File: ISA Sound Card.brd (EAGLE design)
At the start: 175.9 x 108.6 mm, 60 parts, among them IC1 74LS07D, IC2 74AHC1G07DBV, U1 PCM1808, U10 SN74LVC16T245DGGR, U11 SN74LVC16T245DGGR, U12 SN74LVC16T245DGGR, U3 MIC5365-3.3YD5-TR, U4 PCM5102, U5 SN74LVC16T245DGGR, U7 MIC5365-3.3YD5-TR, U8 SN74LVC16T245DGGR, U9 SN74LVC16T245DGGR, X2 LINE_OUT, X3 LINE_IN

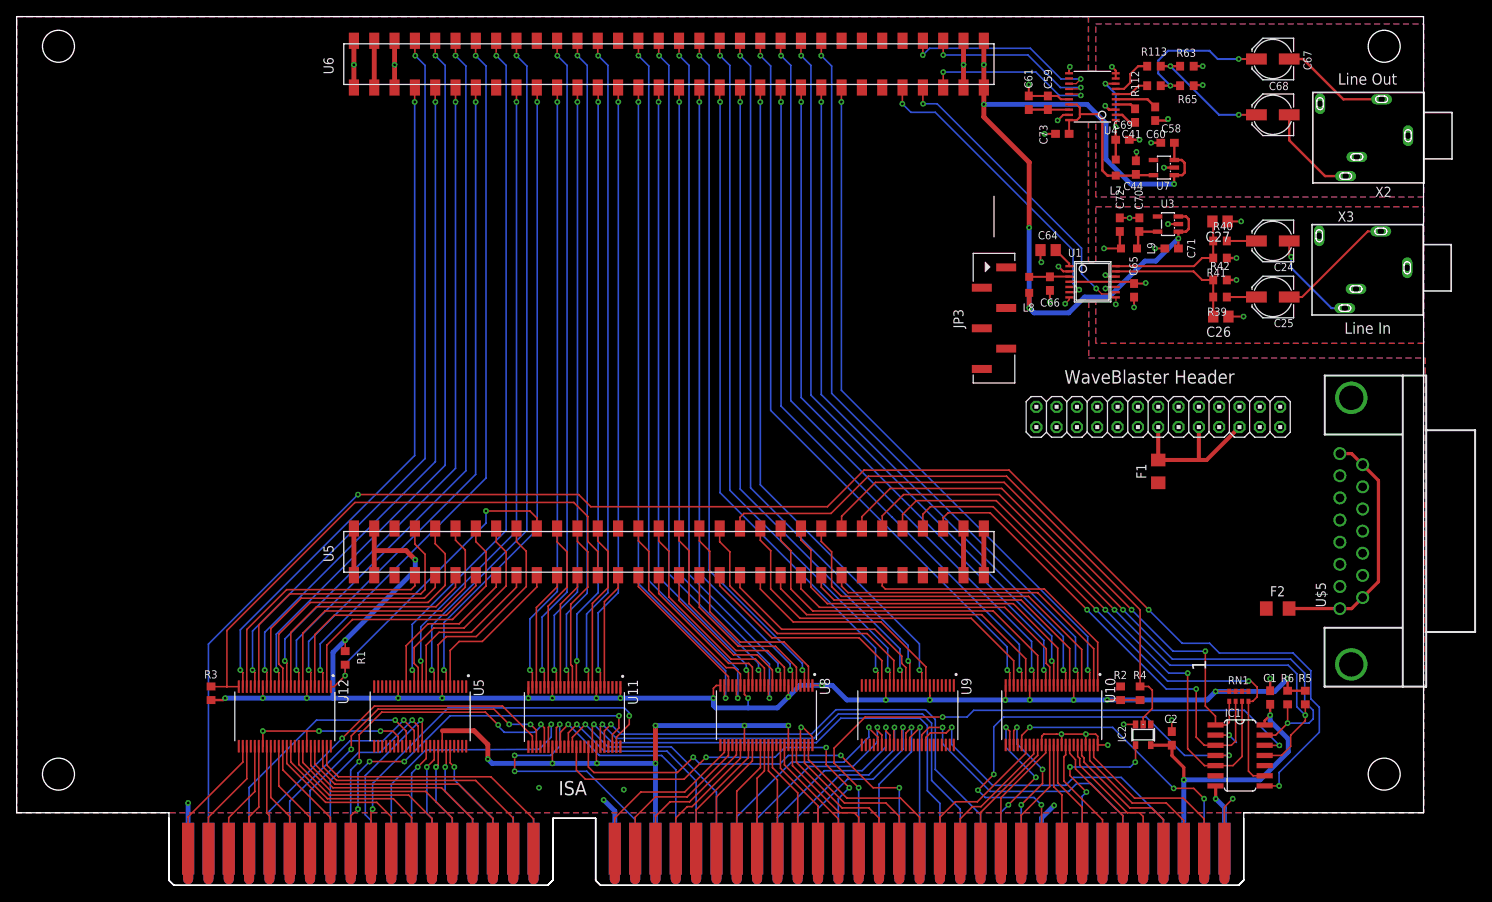
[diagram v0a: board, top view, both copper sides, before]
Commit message: First routing done, DRC passed. MIDI and Waveblaster are todo
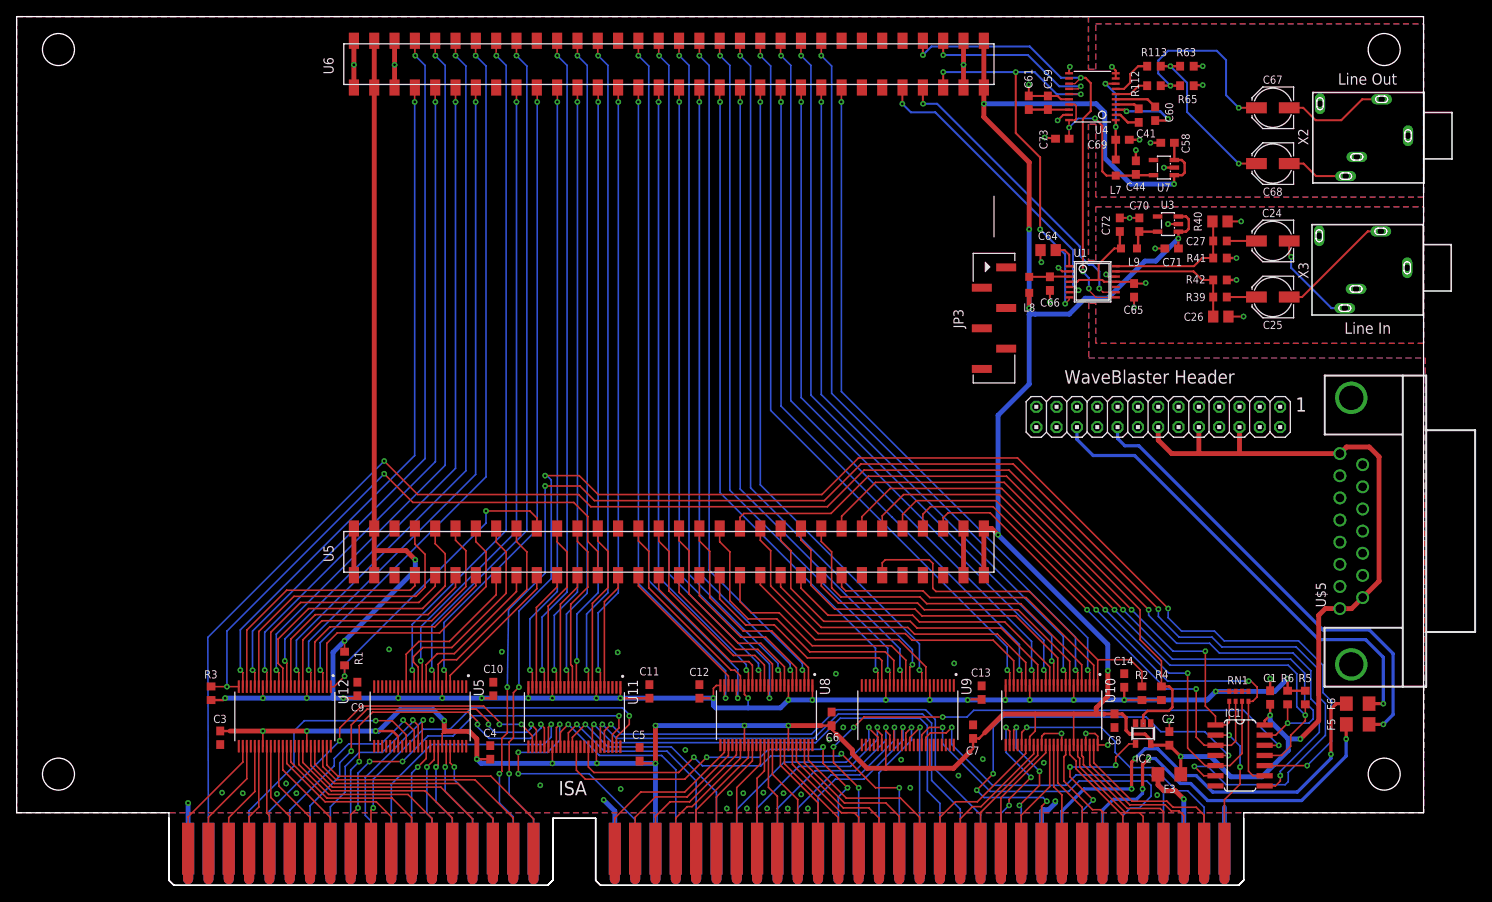
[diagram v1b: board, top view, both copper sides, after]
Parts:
- removed F1, F2: 500mA, adafruit:R1206
- added C10, C11, C12, C13, C14, C3, C4, C5, C6, C7, C8, C9: 100nF, rcl:C0603
- added F3, F5, F6: 500mA, adafruit:R1206
- moved C67 6.10 mm to (165.0, 105.5)
- moved C68 6.10 mm to (165.0, 98.5)
- moved R2 2.67 mm to (148.6, 32.3)
- moved R4 2.67 mm to (151.0, 32.3)
- moved C73 0.61 mm to (138.6, 101.6)
- moved C41 0.46 mm to (148.2, 104.5)
- moved C2 0.30 mm to (152.0, 26.7)
- moved IC2 0.15 mm to (148.7, 27.3)
- moved R1 0.11 mm to (48.9, 36.7)
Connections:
- net -5V renamed -5VDC
- new net MIDI_RXD: U$5.12
- new net MIDI_TXD: U$5.15
- new net N$13: F3.2, ISA.B3
- new net N$14: F5.2, ISA.B7
- new net N$27: F6.2, ISA.B9
- net +12V: now also F5.1; no longer ISA.B7
- net +3V3: now also C10.1, C11.1, C12.1, C13.1, C14.1, C9.1
- net +5V: now also C3.1, C4.1, C5.1, C6.1, C7.1, C8.1, F3.1, JP1.10, JP1.14, JP1.6, U$5.1, U$5.8, U$5.9; no longer F1.2, F2.2, ISA.B3
- net -12V: now also F6.1; no longer ISA.B9
- net GND: now also C10.2, C11.2, C12.2, C13.2, C14.2, C3.2, C4.2, C5.2, C6.2, C7.2, C8.2, C9.2; no longer U$5.12
- net N$5: now also U$1.1; no longer F1.1, JP1.10, JP1.14, JP1.6
- net N$6: now also U$1.5; no longer F2.1, U$5.1, U$5.15, U$5.8, U$5.9
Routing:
- net +5V: track 244.5 -> 467.2 mm, vias 18 -> 21
- net I/!OCS16: track 3.99 -> 191.1 mm, vias 0 -> 5
- net !MEMCS16: track 3.73 -> 181.6 mm, vias 0 -> 5
- net +3V3: track 219.3 -> 286.7 mm, vias 23 -> 26
- net -12V: track 0.00 -> 58.7 mm, vias 0 -> 1
- net +12V: track 0.00 -> 58.1 mm, vias 0 -> 1
- net N$27: track 0.00 -> 55.9 mm, vias 0 -> 3
- net N$14: track 0.00 -> 48.5 mm, vias 0 -> 3
- net N$6: track 31.4 -> 0.00 mm
- net I2S_LRCK: track 22.9 -> 54.3 mm, vias 3 -> 5
- net I2S_BCK: track 26.0 -> 57.2 mm, vias 3 -> 4
- net N$5: track 20.1 -> 0.00 mm
- net GND: track 118.6 -> 105.6 mm, vias 40 -> 66
- net N$13: track 0.00 -> 11.5 mm, vias 0 -> 1
- net FPGA_SD70_DIR: track 36.6 -> 46.9 mm
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
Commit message: Had to change IRQ/DRQ buffers for muxes. Not routed yet
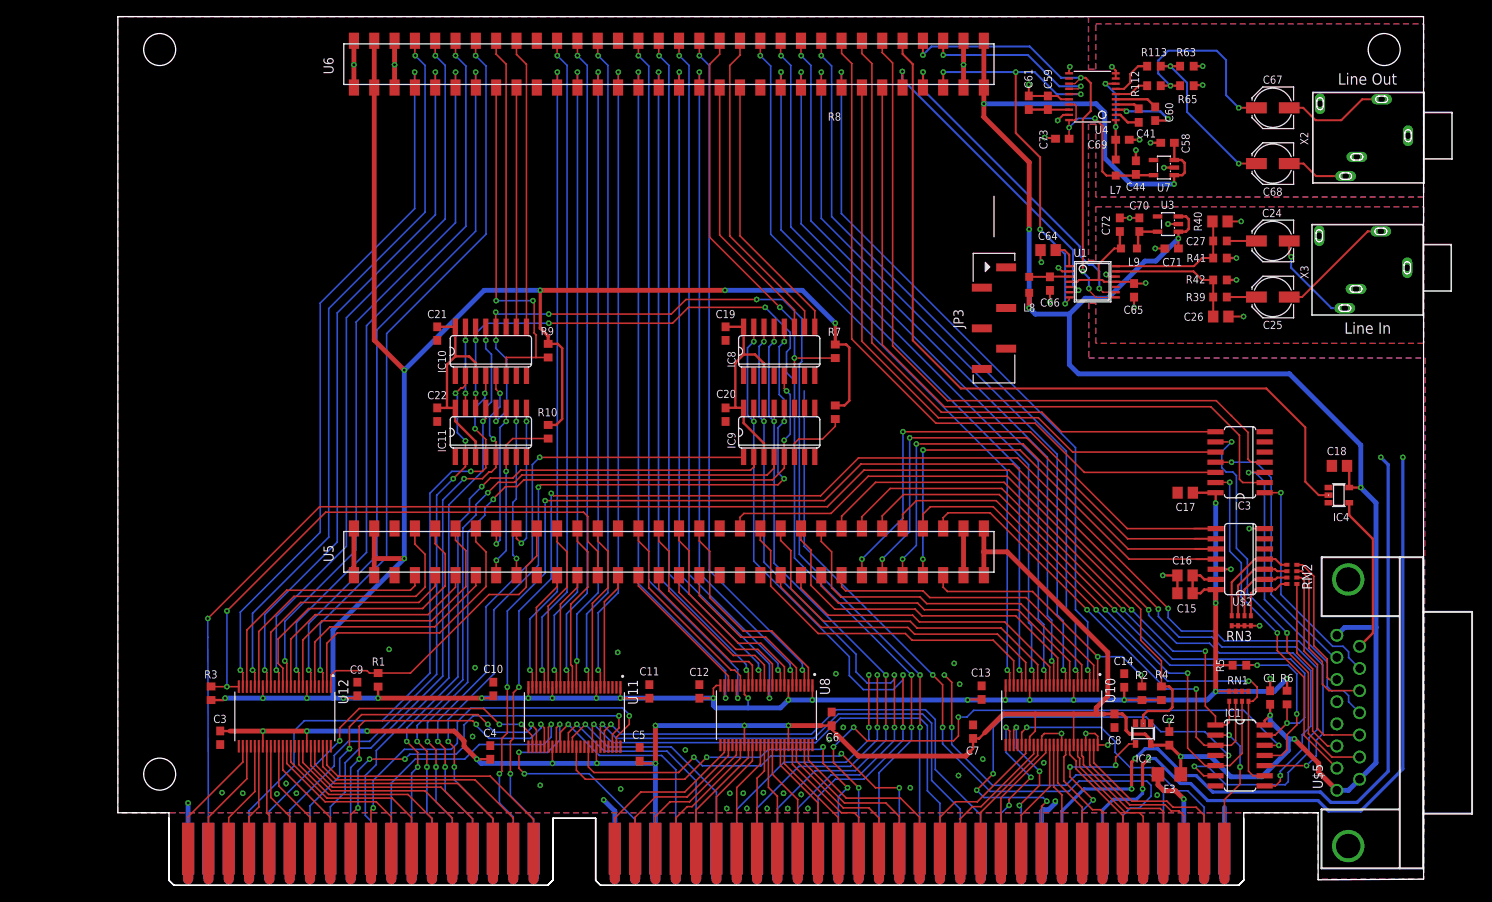
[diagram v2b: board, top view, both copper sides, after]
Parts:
- removed F5, F6: 500mA, adafruit:R1206
- removed JP1: (no value), pinhead:2X13
- removed U5, U9: SN74LVC16T245DGGR, SN74LVC16T245DGGR:SOP50P810X120-48N
- added C15, C16, C17, C18: 100nF, rcl:C0805
- added C19, C20, C21, C22: 100nF, rcl:C0603
- added IC10, IC11, IC8, IC9: 4051D, 40xx:SO16
- added IC3: 74AC14D, 74xx-eu:SO14
- added IC4: 74LVC1G125DBV, 74xx-little-de:SOT23-5
- added R10, R7, R8, R9: 4K7, rcl:R0603
- added RN2: 10K, resistor-dil:0603-ARC
- added RN3: 2K2, resistor-dil:0603-ARC
- added U$2: MCP3004, adafruit:SO14
- RN1: value (none) -> 2K2
- moved U$5 22.7 mm to (174.4, 29.9)
- moved R5 9.17 mm to (160.8, 35.8), turned to 0 degrees
- moved R1 4.97 mm to (53.1, 34.0), turned to 90 degrees
- moved R6 0.08 mm to (166.7, 31.8)
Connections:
- net N$5 renamed FPGA_DCLK
- net N$6 renamed FPGA_ADS0
- removed net +12V: F5.1, JP1.18
- removed net -12V: F6.1, JP1.22
- removed net FPGA_DRQ0: U$1.U6_17, U5.12
- removed net FPGA_DRQ1: U$1.U5_39, U9.13
- removed net FPGA_DRQ2: U$1.U6_41, U9.9
- removed net FPGA_DRQ3: U$1.U6_40, U9.12
- removed net FPGA_DRQ5: U$1.U5_16, U5.13
- removed net FPGA_DRQ6: U$1.U6_16, U5.14
- removed net FPGA_DRQ7: U$1.U5_15, U5.16
- removed net FPGA_IRQ10: U$1.U5_19, U5.5
- removed net FPGA_IRQ11: U$1.U6_19, U5.6
- removed net FPGA_IRQ12: U$1.U5_18, U5.8
- removed net FPGA_IRQ14: U$1.U5_17, U5.11
- removed net FPGA_IRQ15: U$1.U6_18, U5.9
- removed net FPGA_IRQ3: U$1.U6_37, U9.20
- removed net FPGA_IRQ4: U$1.U5_37, U9.19
- removed net FPGA_IRQ5: U$1.U6_38, U9.17
- removed net FPGA_IRQ6: U$1.U5_38, U9.16
- removed net FPGA_IRQ7: U$1.U6_39, U9.14
- removed net FPGA_IRQ9: U$1.U5_41, U9.8
- removed net GAME_B1_N: U$5.2
- removed net GAME_B2_N: U$5.7
- removed net GAME_B3_N: U$5.10
- removed net GAME_B4_N: U$5.14
- removed net GAME_X1: U$5.3
- removed net GAME_X2: U$5.11
- removed net GAME_Y: U$5.13
- removed net GAME_Y1: U$5.6
- removed net N$10: U$1.U5_55
- removed net N$12: U$1.U5_51
- removed net N$16: U$1.U6_51
- removed net N$17: U$1.U6_53
- removed net N$18: U$1.U6_50
- removed net N$19: U$1.U6_52
- removed net N$20: U$1.U6_54
- removed net N$26: U$1.U6_56
- removed net N$3: U$1.U5_59
- removed net N$4: U$1.U5_57
- removed net N$7: U$1.U6_15
- removed net WAVL: JP1.20
- removed net WAVR: JP1.24
- removed net WAV_MIDI: JP1.4
- removed net WAV_RST_N: JP1.26
- new net DRQ_HI_SEL_A0: IC11.11, U$1.U5_16
- new net DRQ_HI_SEL_A1: IC11.10, U$1.U5_17
- new net DRQ_HI_SEL_A2: IC11.9, U$1.U5_18
- new net DRQ_HI_TRIG_N: IC11.6, R10.1, U$1.U5_15
- new net DRQ_LO_SEL_A0: IC10.11, U$1.U6_16
- new net DRQ_LO_SEL_A1: IC10.10, U$1.U6_17
- new net DRQ_LO_SEL_A2: IC10.9, U$1.U6_18
- new net DRQ_LO_TRIG_N: IC10.6, R9.1, U$1.U6_15
- new net FPGA_JOY_B1: IC3.12, U$1.U6_50
- new net FPGA_JOY_B2: IC3.10, U$1.U6_51
- new net FPGA_JOY_B3: IC3.8, U$1.U6_52
- new net FPGA_JOY_B4: IC3.2, U$1.U6_53
- new net FPGA_MIDI_RXD: IC3.4, U$1.U6_54
- new net FPGA_MIDI_TXD: IC4.2, U$1.U6_56
- new net IRQ_HI_SEL_A0: IC9.11, U$1.U5_38
- new net IRQ_HI_SEL_A1: IC9.10, U$1.U5_39
- new net IRQ_HI_SEL_A2: IC9.9, U$1.U5_41
- new net IRQ_HI_TRIG_N: IC9.6, R8.1, U$1.U5_37
- new net IRQ_LO_SEL_A0: IC8.11, U$1.U6_37
- new net IRQ_LO_SEL_A1: IC8.10, U$1.U6_40
- new net IRQ_LO_SEL_A2: IC8.9, U$1.U6_39
- new net IRQ_LO_TRIG_N: IC8.6, R7.1, U$1.U6_38
- new net JOY_B1_N: IC3.13, U$5.2
- new net JOY_B2_N: IC3.11, U$5.7
- new net JOY_B3_N: IC3.9, U$5.10
- new net JOY_B4_N: IC3.1, U$5.14
- new net JOY_CLK: U$1.U5_57, U$2.11
- new net JOY_CS_N: U$1.U5_51, U$2.8
- new net JOY_DIN: U$1.U5_53, U$2.9
- new net JOY_DOUT: U$1.U5_55, U$2.10
- new net JOY_X1: RN2.1, U$5.3
- new net JOY_X2: RN2.2, U$5.11
- new net JOY_Y1: RN2.4, U$5.6
- new net JOY_Y2: RN2.3, U$5.13
- new net N$15: RN2.5, RN3.8, U$2.4
- new net N$28: RN2.6, RN3.7, U$2.3
- new net N$31: RN2.7, RN3.6, U$2.2
- new net N$32: RN2.8, RN3.5, U$2.1
- new net N$34: IC3.6
- new net N$41: IC3.5
- net +3V3: now also C15.1, C16.1, C17.1, IC3.14, R10.2, R7.2, R8.2, R9.2, U$2.13, U$2.14; no longer U5.18, U5.7, U9.18, U9.7
- net +5V: now also C18.1, C19.1, C20.1, C21.1, C22.1, IC10.16, IC10.3, IC11.16, IC11.3, IC4.5, IC8.16, IC8.3, IC9.16, IC9.3; no longer JP1.10, JP1.14, JP1.6, U5.31, U5.42, U9.31, U9.42
- net DRQ0: now also IC10.13, IC11.13; no longer U5.37
- net DRQ1: now also IC10.14, IC11.14; no longer U9.36
- net DRQ2: now also IC10.15, IC11.15; no longer U9.40
- net DRQ3: now also IC10.12, IC11.12; no longer U9.37
- net DRQ5: now also IC10.5, IC11.5; no longer U5.36
- net DRQ6: now also IC10.2, IC11.2; no longer U5.35
- net DRQ7: now also IC10.4, IC11.4; no longer U5.33
- net FPGA_SD70_DIR: now also U$1.U5_59; no longer U$1.U5_53
- net GND: now also C15.2, C16.2, C17.2, C18.2, C19.2, C20.2, C21.2, C22.2, IC10.7, IC10.8, IC11.7, IC11.8, IC3.7, IC4.1, IC4.3, IC8.7, IC8.8, IC9.7, IC9.8, RN3.1, RN3.2, RN3.3, RN3.4, U$2.12, U$2.7; no longer JP1.1, JP1.11, JP1.15, JP1.17, JP1.19, JP1.21, JP1.23, JP1.25, JP1.3, JP1.5, JP1.7, JP1.9, U5.1, U5.10, U5.15, U5.21, U5.24, U5.25, U5.28, U5.34, U5.39, U5.4, U5.45, U5.48, U9.1, U9.10, U9.15, U9.21, U9.24, U9.25, U9.28, U9.34, U9.39, U9.4, U9.45, U9.48
- net IRQ10: now also IC8.12, IC9.12; no longer U5.44
- net IRQ11: now also IC8.1, IC9.1; no longer U5.43
- net IRQ12: now also IC8.5, IC9.5; no longer U5.41
- net IRQ14: now also IC8.2, IC9.2; no longer U5.38
- net IRQ15: now also IC8.4, IC9.4; no longer U5.40
- net IRQ3: no longer U9.29
- net IRQ4: no longer U9.30
- net IRQ5: now also IC8.13, IC9.13; no longer U9.32
- net IRQ6: now also IC8.14, IC9.14; no longer U9.33
- net IRQ7: now also IC8.15, IC9.15; no longer U9.35
- net IRQ9: no longer U9.41
- net MIDI_RXD: now also IC3.3
- net MIDI_TXD: now also IC4.4
- net N$14: no longer F5.2
- net N$27: no longer F6.2
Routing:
- net +3V3: track 286.7 -> 413.8 mm, vias 26 -> 28
- net DRQ3: track 17.9 -> 129.2 mm, vias 1 -> 7
- net DRQ1: track 19.3 -> 125.8 mm, vias 1 -> 6
- net FPGA_MIDI_TXD: track 0.00 -> 101.9 mm
- net FPGA_MIDI_RXD: track 0.00 -> 93.2 mm
- net FPGA_JOY_B4: track 0.00 -> 90.3 mm
- net FPGA_JOY_B1: track 0.00 -> 90.2 mm
- net IRQ10: track 15.0 -> 105.2 mm, vias 1 -> 6
- net FPGA_DRQ3: track 89.6 -> 0.00 mm, vias 2 -> 0
- net FPGA_IRQ5: track 89.4 -> 0.00 mm, vias 2 -> 0
- net FPGA_IRQ15: track 86.3 -> 0.00 mm, vias 2 -> 0
- net FPGA_DRQ6: track 86.2 -> 0.00 mm, vias 2 -> 0
- net FPGA_JOY_B3: track 0.00 -> 85.8 mm
- net IRQ12: track 13.8 -> 98.6 mm, vias 1 -> 5
- net FPGA_IRQ7: track 83.1 -> 0.00 mm, vias 2 -> 0
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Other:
- board size 175.9 x 108.6 mm -> 163.2 x 108.6 mm
- board text removed: "1"
- board text removed: "WaveBlaster Header"

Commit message: Routing done. Fixed two missing signals. Five proto PCBs being made by JLC
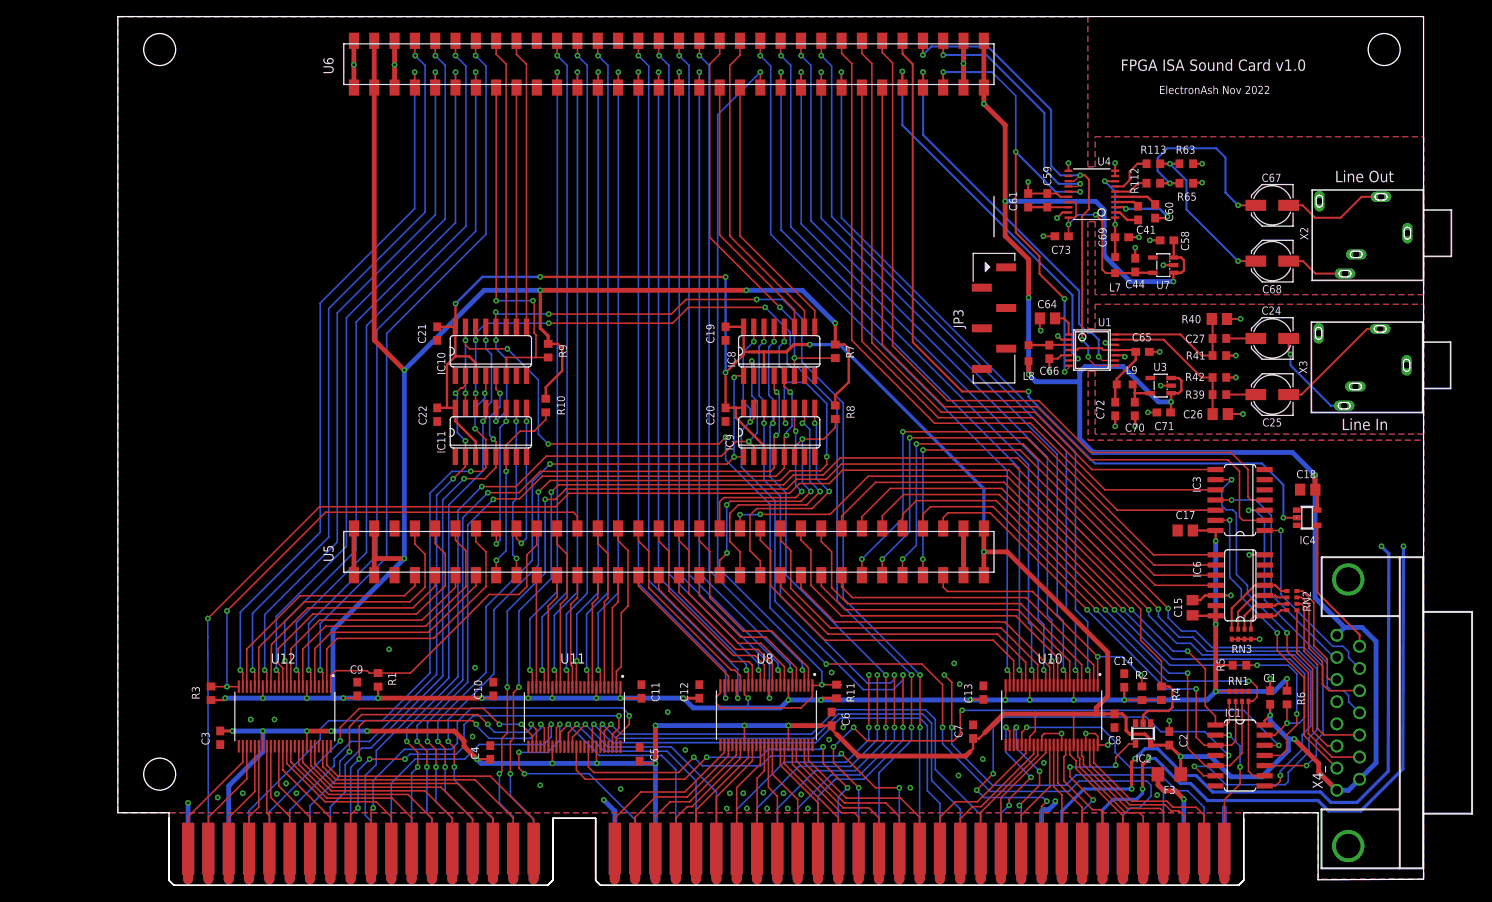
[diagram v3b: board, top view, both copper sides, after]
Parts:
- removed C16: 100nF, rcl:C0805
- removed U$2: MCP3004, adafruit:SO14
- added IC6: MCP3004, adafruit:SO14
- added R11: 4K7, rcl:R0603
- moved C70 23.0 mm to (147.7, 67.8), turned to 270 degrees
- moved C72 23.0 mm to (145.3, 67.8), turned to 90 degrees
- moved C71 20.5 mm to (151.3, 67.4)
- moved U3 20.2 mm to (150.9, 70.8)
- moved L9 17.0 mm to (146.4, 70.9)
- moved C25 12.2 mm to (164.9, 69.6)
- moved C26 12.2 mm to (158.4, 67.2)
- moved C41 12.2 mm to (148.1, 92.3)
- moved C44 12.2 mm to (147.8, 85.8)
- moved C58 12.2 mm to (151.7, 88.9)
- moved C59 12.2 mm to (136.8, 93.9)
- moved C61 12.2 mm to (134.4, 93.9)
- moved C67 12.2 mm to (164.9, 93.3)
- moved C69 12.2 mm to (146.1, 89.3)
- moved L7 12.2 mm to (145.2, 85.8)
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- renumbered U$5 to X4_
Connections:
- removed net +5VDC: ISA.D16
- removed net FPGA_MEMW_R: U11.3
- removed net N$11: U$1.U5_28
- removed net N$41: IC3.5
- new net FPGA_MEMW_N: U$1.U5_27, U11.3
- new net FPGA_SA159_DIR: R11.2, U$1.U6_41, U8.1, U8.24
- net +3V3: now also IC6.13, IC6.14, R11.1; no longer C16.1, U$2.13, U$2.14, U8.1, U8.24
- net +5V: now also ISA.D16
- net FPGA_BALE: now also U$1.U5_22; no longer U$1.U5_23
- net FPGA_DACK0_N: now also U$1.U5_21; no longer U$1.U5_22
- net FPGA_DACK2_N: now also U$1.U5_23; no longer U$1.U5_24
- net FPGA_DACK3_N: now also U$1.U5_25; no longer U$1.U5_26
- net FPGA_DACK6_N: now also U$1.U5_19; no longer U$1.U5_21
- net FPGA_IOW_N: now also U$1.U5_26; no longer U$1.U5_27
- net FPGA_MEMR_N: now also U$1.U5_28
- net FPGA_SD159_DIR: now also U$1.U5_24; no longer U$1.U5_25
- net GND: now also IC3.5, IC6.12, IC6.7; no longer C16.2, U$2.12, U$2.7
- net JOY_CLK: now also IC6.11; no longer U$2.11
- net JOY_CS_N: now also IC6.8; no longer U$2.8
- net JOY_DIN: now also IC6.9; no longer U$2.9
- net JOY_DOUT: now also IC6.10; no longer U$2.10
- net N$15: now also IC6.4; no longer U$2.4
- net N$28: now also IC6.3; no longer U$2.3
- net N$31: now also IC6.2; no longer U$2.2
- net N$32: now also IC6.1; no longer U$2.1
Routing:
- net FPGA_SA159_DIR: track 0.00 -> 107.0 mm, vias 0 -> 2
- net +5V: track 504.2 -> 607.8 mm, vias 19 -> 28
- net DRQ2: track 100.7 -> 148.6 mm, vias 4 -> 7
- net IRQ_HI_SEL_A1: track 0.00 -> 32.2 mm, vias 0 -> 2
- net IRQ_HI_SEL_A2: track 0.00 -> 30.4 mm, vias 0 -> 2
- net IRQ_HI_TRIG_N: track 8.59 -> 35.8 mm, vias 0 -> 4
- net IRQ_HI_SEL_A0: track 0.00 -> 25.0 mm, vias 0 -> 2
- net FPGA_MEMR_N: track 0.00 -> 21.0 mm
- net +3V3: track 413.8 -> 396.2 mm
- net IRQ14: track 86.3 -> 100.7 mm, vias 3 -> 5
- net FPGA_MEMW_N: track 0.00 -> 14.3 mm
- net IRQ10: track 105.2 -> 117.7 mm
- net N$14: track 91.0 -> 79.8 mm
- net N$27: track 94.7 -> 83.6 mm
- net IRQ15: track 87.4 -> 98.0 mm, vias 3 -> 5
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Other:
- board text added: "ElectronAsh Nov 2022"
- board text added: "FPGA ISA Sound Card v1.0"
